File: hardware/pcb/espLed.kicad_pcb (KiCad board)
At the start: 2 copper layers, 32.3 x 36.6 mm, 23 parts, among them J1 led_strip, J2 flashing, J3 power, Q1 IRF9310TRPBF, Q2 AO3400A, Q3 AO3400A, Q4 AO3400A, SW1 reset, SW2 flash, U1 AMS1117-3.3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

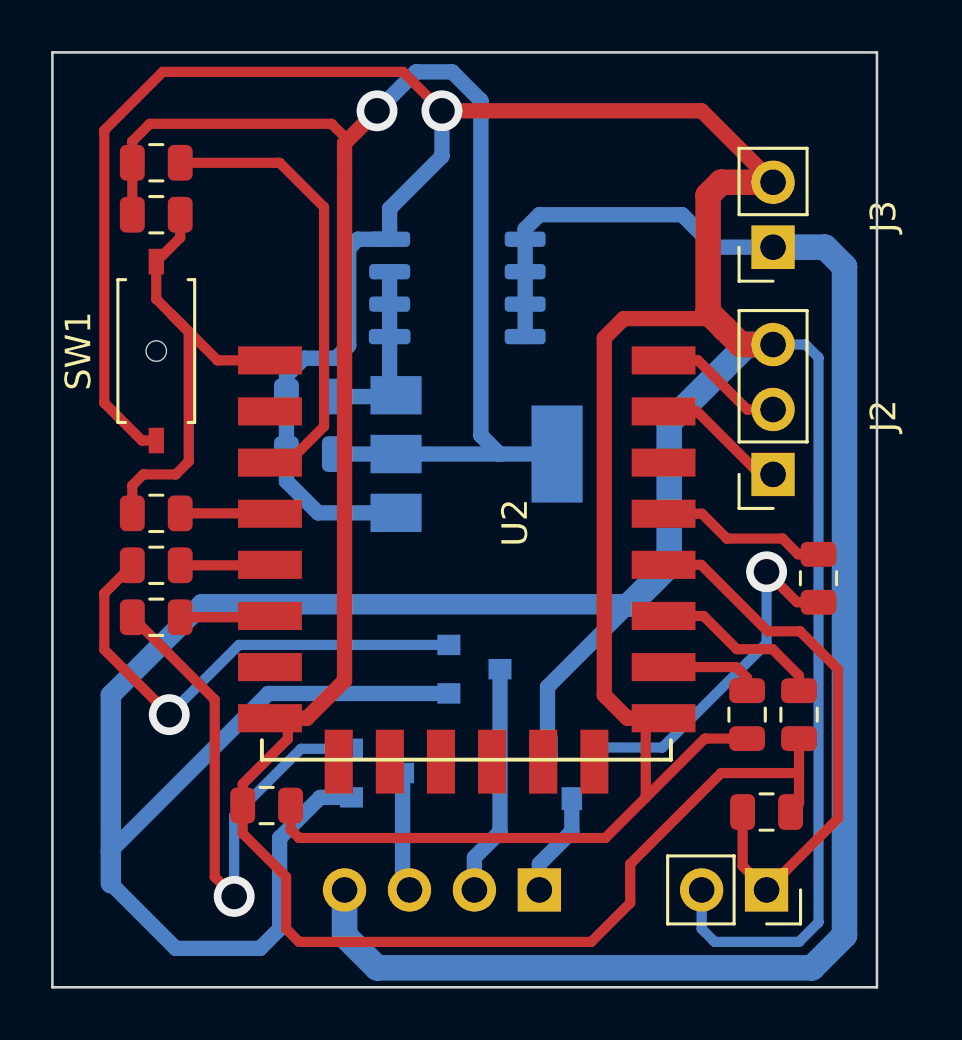
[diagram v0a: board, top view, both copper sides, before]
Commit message: reroute GND of the 'flash' jumper to fit leds' 12v tighter
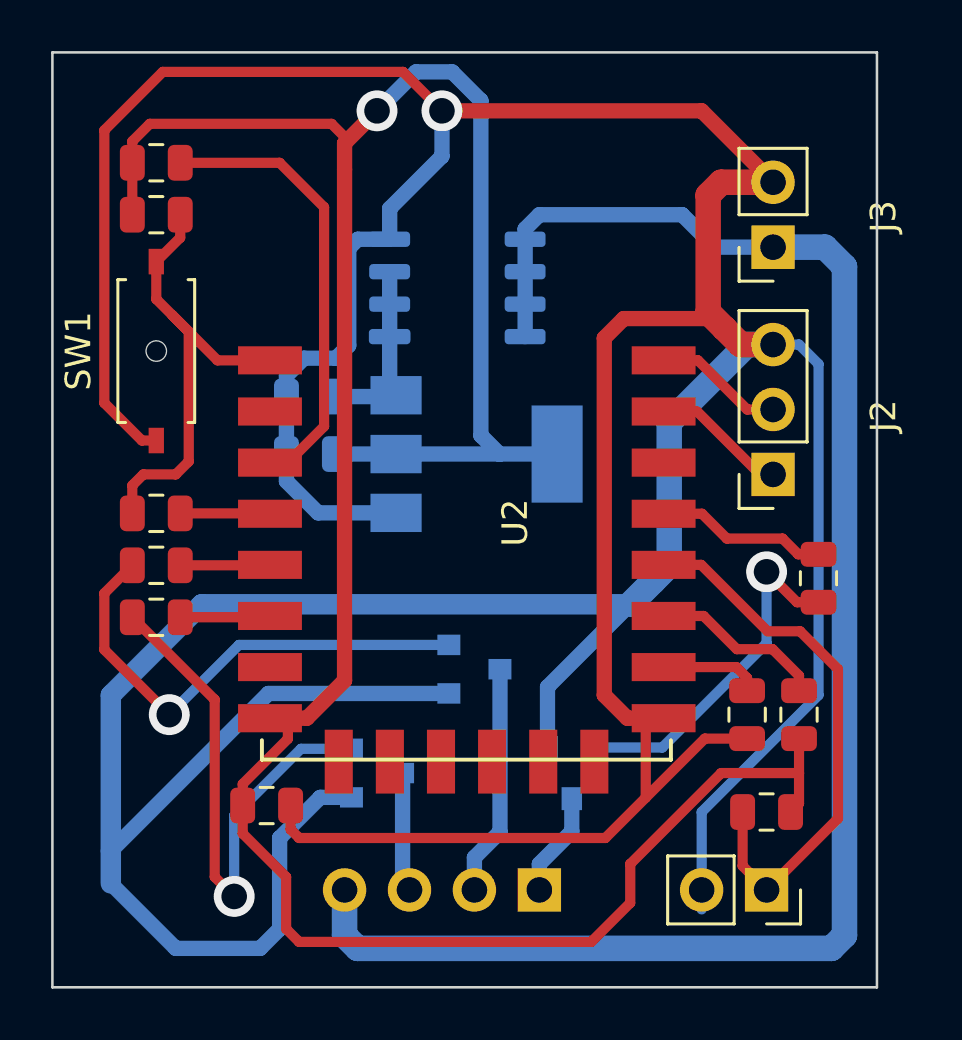
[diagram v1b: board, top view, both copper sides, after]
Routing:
- net GND: track 233.4 -> 227.3 mm
- net /12v_in: track 66.3 -> 65.7 mm
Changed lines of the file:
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@@
     (thickness 1.6)
     (drawings 6)
-    (tracks 207)
+    (tracks 205)
     (zones 0)
     (modules 23)
@@
   )
   (setup
-    (last_trace_width 0.6)
+    (last_trace_width 0.4)
     (user_trace_width 0.4)
     (user_trace_width 0.6)
@@
   (segment (start 188.590501 133.0175) (end 186.28 135.328001) (width 0.4) (layer F.Cu) (net 1))
   (segment (start 190.246 133.0175) (end 188.590501 133.0175) (width 0.4) (layer F.Cu) (net 1))
-  (segment (start 192.532 117.602) (end 191.262 117.602) (width 0.4) (layer B.Cu) (net 1))
-  (segment (start 193.04 118.11) (end 192.532 117.602) (width 0.4) (layer B.Cu) (net 1))
-  (segment (start 193.04 140.208) (end 193.04 118.11) (width 0.4) (layer B.Cu) (net 1))
-  (segment (start 192.278 140.97) (end 193.04 140.208) (width 0.4) (layer B.Cu) (net 1))
-  (segment (start 188.976 140.97) (end 192.278 140.97) (width 0.4) (layer B.Cu) (net 1))
-  (segment (start 188.468 140.462) (end 188.976 140.97) (width 0.4) (layer B.Cu) (net 1))
-  (segment (start 188.468 138.938) (end 188.468 140.462) (width 0.4) (layer B.Cu) (net 1))
   (segment (start 189.23 111.252) (end 191.262 111.252) (width 1) (layer F.Cu) (net 1))
   (segment (start 188.722 111.76) (end 189.23 111.252) (width 1) (layer F.Cu) (net 1))
@@
   (segment (start 165.354 137.414) (end 165.354 131.318) (width 0.8) (layer B.Cu) (net 1))
   (segment (start 165.354 138.684) (end 165.354 137.414) (width 0.8) (layer B.Cu) (net 1))
+  (segment (start 193.04 131.318) (end 188.468 135.89) (width 0.4) (layer B.Cu) (net 1))
+  (segment (start 188.468 135.89) (end 188.468 138.938) (width 0.4) (layer B.Cu) (net 1))
+  (segment (start 193.04 118.364) (end 193.04 131.318) (width 0.4) (layer B.Cu) (net 1))
+  (segment (start 192.278 117.602) (end 193.04 118.364) (width 0.4) (layer B.Cu) (net 1))
+  (segment (start 191.262 117.602) (end 192.278 117.602) (width 0.4) (layer B.Cu) (net 1))
   (segment (start 174.0995 119.636) (end 176.462 119.636) (width 0.6) (layer B.Cu) (net 2))
   (segment (start 176.262 117.291) (end 176.262 114.751) (width 0.6) (layer B.Cu) (net 2))
@@
   (segment (start 188.292 120.22) (end 190.754 122.682) (width 0.4) (layer F.Cu) (net 8))
   (segment (start 186.28 120.22) (end 188.292 120.22) (width 0.4) (layer F.Cu) (net 8))
-  (segment (start 175.768 141.986) (end 174.498 140.716) (width 1) (layer B.Cu) (net 9))
-  (segment (start 192.786 141.986) (end 175.768 141.986) (width 1) (layer B.Cu) (net 9))
-  (segment (start 194.056 140.716) (end 192.786 141.986) (width 1) (layer B.Cu) (net 9))
-  (segment (start 194.056 114.554) (end 194.056 140.716) (width 1) (layer B.Cu) (net 9))
-  (segment (start 174.498 140.716) (end 174.498 138.938) (width 1) (layer B.Cu) (net 9))
-  (segment (start 193.294 113.792) (end 194.056 114.554) (width 1) (layer B.Cu) (net 9))
-  (segment (start 191.262 113.792) (end 193.294 113.792) (width 1) (layer B.Cu) (net 9))
   (segment (start 181.562 113.481) (end 181.562 117.291) (width 0.6) (layer B.Cu) (net 9))
   (segment (start 181.562 113.078) (end 181.562 113.481) (width 0.6) (layer B.Cu) (net 9))
@@
   (segment (start 187.706 112.522) (end 182.118 112.522) (width 0.6) (layer B.Cu) (net 9))
   (segment (start 191.262 113.792) (end 188.976 113.792) (width 0.6) (layer B.Cu) (net 9))
+  (segment (start 174.498 140.716) (end 174.498 138.938) (width 1) (layer B.Cu) (net 9))
+  (segment (start 175.006 141.224) (end 174.498 140.716) (width 1) (layer B.Cu) (net 9))
+  (segment (start 193.548 141.224) (end 175.006 141.224) (width 1) (layer B.Cu) (net 9))
+  (segment (start 194.056 114.554) (end 194.056 140.716) (width 1) (layer B.Cu) (net 9))
+  (segment (start 193.294 113.792) (end 194.056 114.554) (width 1) (layer B.Cu) (net 9))
+  (segment (start 194.056 140.716) (end 193.548 141.224) (width 1) (layer B.Cu) (net 9))
+  (segment (start 191.262 113.792) (end 193.294 113.792) (width 1) (layer B.Cu) (net 9))
   (via (at 191.008 126.492) (size 1.6) (drill 1) (layers F.Cu B.Cu) (net 10))
   (segment (start 192.1995 127.6835) (end 191.008 126.492) (width 0.4) (layer F.Cu) (net 10))

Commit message: fix the board outline
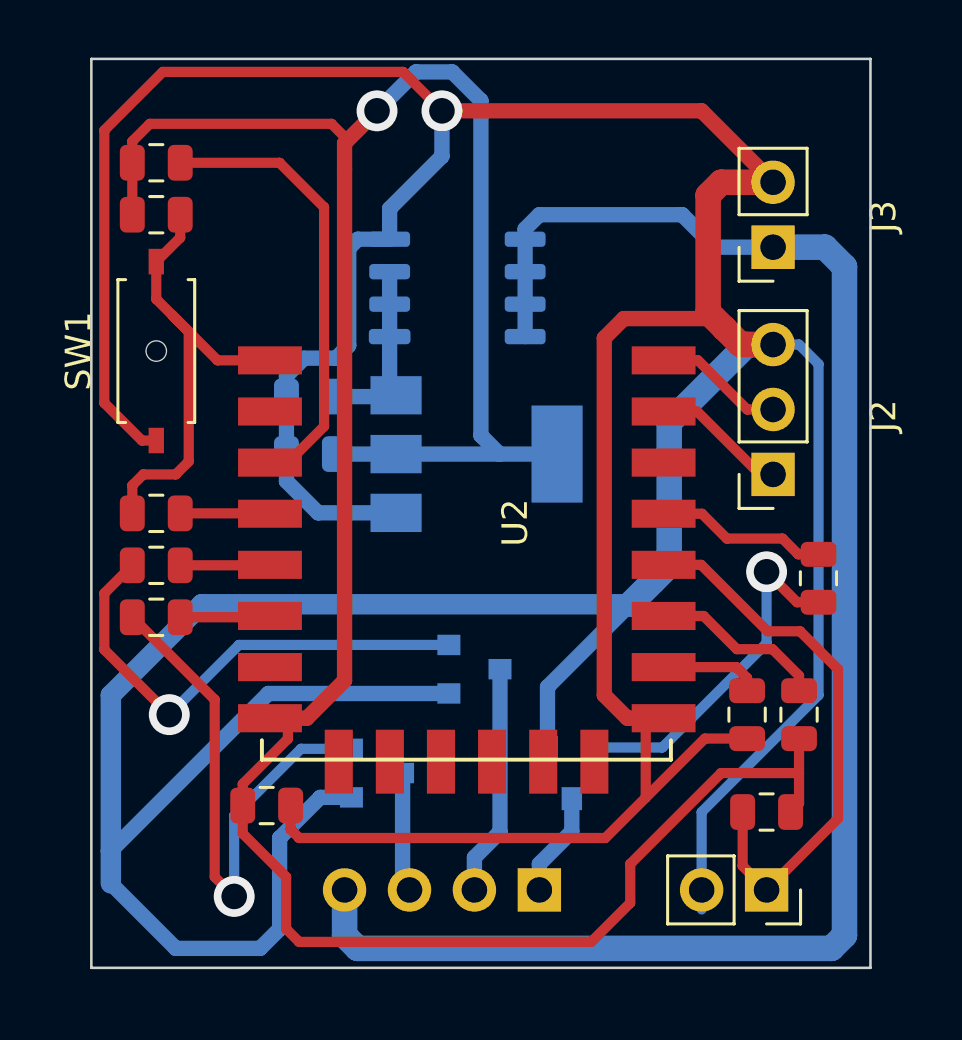
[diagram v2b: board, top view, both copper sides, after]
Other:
- board size 32.3 x 36.6 mm -> 30.5 x 35.6 mm
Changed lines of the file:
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@@
     )
   )
-  (dimension 36.576 (width 0.15) (layer Dwgs.User)
-    (gr_text "36,576 mm" (at 199.674 124.46 270) (layer Dwgs.User)
+  (dimension 30.48 (width 0.15) (layer Dwgs.User)
+    (gr_text "30,480 mm" (at 179.832 103.348) (layer Dwgs.User)
       (effects (font (size 1 1) (thickness 0.15)))
     )
-    (feature1 (pts (xy 195.326 142.748) (xy 198.960421 142.748)))
-    (feature2 (pts (xy 195.326 106.172) (xy 198.960421 106.172)))
-    (crossbar (pts (xy 198.374 106.172) (xy 198.374 142.748)))
-    (arrow1a (pts (xy 198.374 142.748) (xy 197.787579 141.621496)))
-    (arrow1b (pts (xy 198.374 142.748) (xy 198.960421 141.621496)))
-    (arrow2a (pts (xy 198.374 106.172) (xy 197.787579 107.298504)))
-    (arrow2b (pts (xy 198.374 106.172) (xy 198.960421 107.298504)))
+    (feature1 (pts (xy 195.072 106.426) (xy 195.072 104.061579)))
+    (feature2 (pts (xy 164.592 106.426) (xy 164.592 104.061579)))
+    (crossbar (pts (xy 164.592 104.648) (xy 195.072 104.648)))
+    (arrow1a (pts (xy 195.072 104.648) (xy 193.945496 105.234421)))
+    (arrow1b (pts (xy 195.072 104.648) (xy 193.945496 104.061579)))
+    (arrow2a (pts (xy 164.592 104.648) (xy 165.718504 105.234421)))
+    (arrow2b (pts (xy 164.592 104.648) (xy 165.718504 104.061579)))
   )
-  (dimension 32.258 (width 0.15) (layer Dwgs.User)
-    (gr_text "32,258 mm" (at 179.197 102.586) (layer Dwgs.User)
+  (dimension 35.56 (width 0.15) (layer Dwgs.User)
+    (gr_text "35,560 mm" (at 198.15 124.206 270) (layer Dwgs.User)
       (effects (font (size 1 1) (thickness 0.15)))
     )
-    (feature1 (pts (xy 195.326 106.172) (xy 195.326 103.299579)))
-    (feature2 (pts (xy 163.068 106.172) (xy 163.068 103.299579)))
-    (crossbar (pts (xy 163.068 103.886) (xy 195.326 103.886)))
-    (arrow1a (pts (xy 195.326 103.886) (xy 194.199496 104.472421)))
-    (arrow1b (pts (xy 195.326 103.886) (xy 194.199496 103.299579)))
-    (arrow2a (pts (xy 163.068 103.886) (xy 164.194504 104.472421)))
-    (arrow2b (pts (xy 163.068 103.886) (xy 164.194504 103.299579)))
+    (feature1 (pts (xy 195.072 141.986) (xy 197.436421 141.986)))
+    (feature2 (pts (xy 195.072 106.426) (xy 197.436421 106.426)))
+    (crossbar (pts (xy 196.85 106.426) (xy 196.85 141.986)))
+    (arrow1a (pts (xy 196.85 141.986) (xy 196.263579 140.859496)))
+    (arrow1b (pts (xy 196.85 141.986) (xy 197.436421 140.859496)))
+    (arrow2a (pts (xy 196.85 106.426) (xy 196.263579 107.552504)))
+    (arrow2b (pts (xy 196.85 106.426) (xy 197.436421 107.552504)))
   )
-  (gr_line (start 195.326 106.172) (end 195.326 142.748) (layer Edge.Cuts) (width 0.1))
-  (gr_line (start 163.068 106.172) (end 195.326 106.172) (layer Edge.Cuts) (width 0.1))
-  (gr_line (start 163.068 142.748) (end 163.068 106.172) (layer Edge.Cuts) (width 0.1))
-  (gr_line (start 195.326 142.748) (end 163.068 142.748) (layer Edge.Cuts) (width 0.1))
+  (gr_line (start 195.072 106.426) (end 195.072 141.986) (layer Edge.Cuts) (width 0.1))
+  (gr_line (start 164.592 106.426) (end 195.072 106.426) (layer Edge.Cuts) (width 0.1))
+  (gr_line (start 164.592 141.986) (end 164.592 106.426) (layer Edge.Cuts) (width 0.1))
+  (gr_line (start 195.072 141.986) (end 164.592 141.986) (layer Edge.Cuts) (width 0.1))
   (segment (start 172.2245 122.9485) (end 172.2245 121.886) (width 0.6) (layer B.Cu) (net 1))
   (segment (start 173.462 124.186) (end 172.2245 122.9485) (width 0.6) (layer B.Cu) (net 1))

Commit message: fix ESP's 3d model and move led connector to the top layer (just visual)
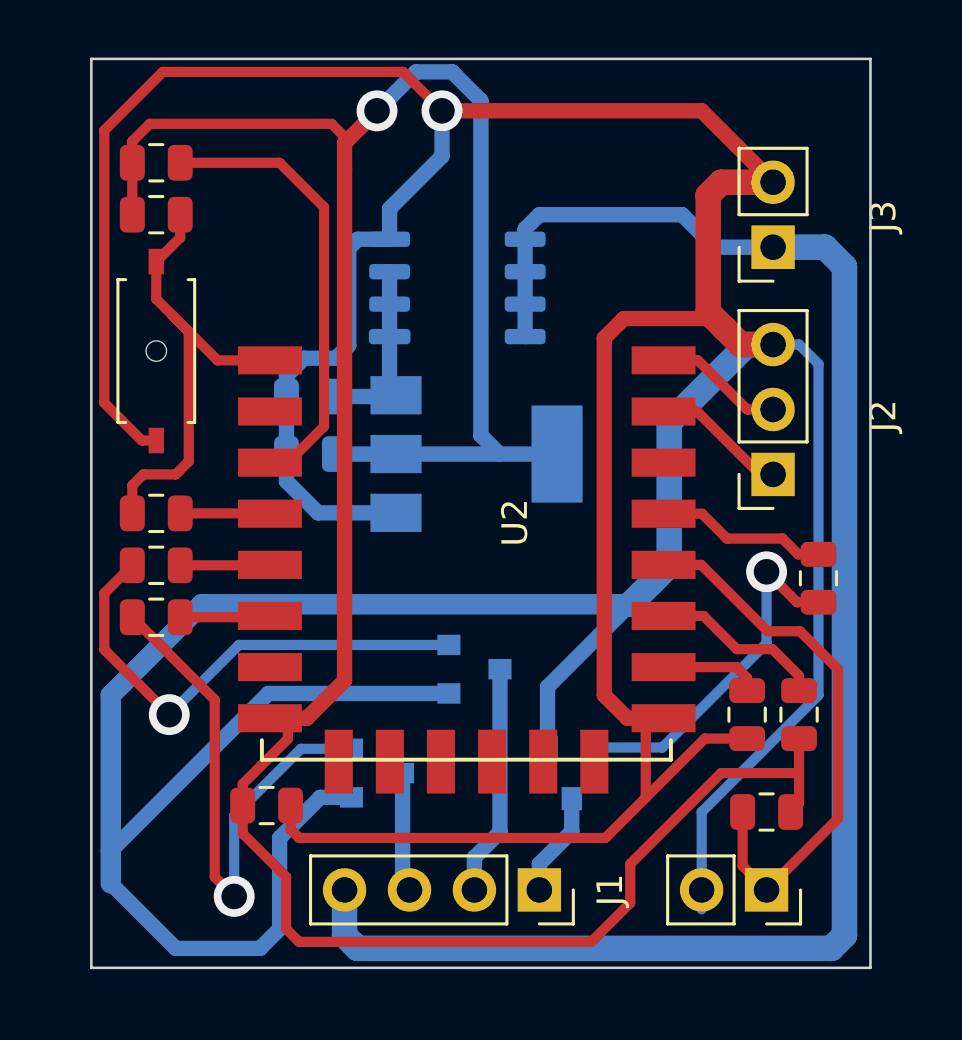
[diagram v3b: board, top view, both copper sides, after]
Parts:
- J1: moved to F.Cu
- turned J1 to 270 degrees
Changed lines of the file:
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@@
+      (rotate (xyz 0 0 0))
+    )
+    (model ${KIPRJMOD}/libs/kicad-ESP8266/ESP8266.3dshapes/ESP-12-E-better.wrl
+      (at (xyz 0 0 0))
+      (scale (xyz 1 1 1))
       (rotate (xyz 0 0 0))
     )
@@
     (tags "Tactile Switch")
     (attr smd)
-    (fp_text reference SW1 (at 0 -3.048 90) (layer F.SilkS)
-      (effects (font (size 1 1) (thickness 0.15)))
-    )
-    (fp_text value reset (at -0.254 -2.286 90) (layer F.Fab)
+    (fp_text reference SW1 (at 0 -3.048 90) (layer F.SilkS) hide
+      (effects (font (size 1 1) (thickness 0.15)))
+    )
+    (fp_text value reset (at -0.254 -2.286 90) (layer F.Fab) hide
       (effects (font (size 1 1) (thickness 0.15)))
     )
@@
     )
   )
-  (module Connector_PinSocket_2.54mm:PinSocket_1x04_P2.54mm_Vertical (layer B.Cu)
-    (at 182.118 138.938 90)
+  (module Connector_PinSocket_2.54mm:PinSocket_1x04_P2.54mm_Vertical (layer F.Cu)
+    (at 182.118 138.938 270)
     (descr "Through hole straight socket strip, 1x04, 2.54mm pitch, single row (from Kicad 4.0.7), script generated")
     (tags "Through hole socket strip THT 1x04 2.54mm single row")
-    (fp_text reference J1 (at 0 2.77 90) (layer B.SilkS)
-      (effects (font (size 1 1) (thickness 0.15)) (justify mirror))
-    )
-    (fp_text value led_strip (at 0 -10.39 90) (layer B.Fab)
-      (effects (font (size 1 1) (thickness 0.15)) (justify mirror))
-    )
-    (fp_line (start -1.27 1.27) (end 0.635 1.27) (layer B.Fab) (width 0.1))
-    (fp_line (start 0.635 1.27) (end 1.27 0.635) (layer B.Fab) (width 0.1))
-    (fp_line (start 1.27 0.635) (end 1.27 -8.89) (layer B.Fab) (width 0.1))
-    (fp_line (start 1.27 -8.89) (end -1.27 -8.89) (layer B.Fab) (width 0.1))
-    (fp_line (start -1.27 -8.89) (end -1.27 1.27) (layer B.Fab) (width 0.1))
-    (fp_line (start -1.33 -1.27) (end 1.33 -1.27) (layer B.SilkS) (width 0.12))
-    (fp_line (start -1.33 -1.27) (end -1.33 -8.95) (layer B.SilkS) (width 0.12))
-    (fp_line (start -1.33 -8.95) (end 1.33 -8.95) (layer B.SilkS) (width 0.12))
-    (fp_line (start 1.33 -1.27) (end 1.33 -8.95) (layer B.SilkS) (width 0.12))
-    (fp_line (start 1.33 1.33) (end 1.33 0) (layer B.SilkS) (width 0.12))
-    (fp_line (start 0 1.33) (end 1.33 1.33) (layer B.SilkS) (width 0.12))
-    (fp_line (start -1.8 1.8) (end 1.75 1.8) (layer B.CrtYd) (width 0.05))
-    (fp_line (start 1.75 1.8) (end 1.75 -9.4) (layer B.CrtYd) (width 0.05))
-    (fp_line (start 1.75 -9.4) (end -1.8 -9.4) (layer B.CrtYd) (width 0.05))
-    (fp_line (start -1.8 -9.4) (end -1.8 1.8) (layer B.CrtYd) (width 0.05))
-    (fp_text user %R (at 0 -3.81 180) (layer B.Fab)
-      (effects (font (size 1 1) (thickness 0.15)) (justify mirror))
-    )
-    (pad 1 thru_hole rect (at 0 0 90) (size 1.7 1.7) (drill 1) (layers *.Cu *.Mask)
+    (fp_text reference J1 (at 0 -2.77 270) (layer F.SilkS)
+      (effects (font (size 1 1) (thickness 0.15)))
+    )
+    (fp_text value led_strip (at 0 10.39 270) (layer F.Fab)
+      (effects (font (size 1 1) (thickness 0.15)))
+    )
+    (fp_line (start -1.27 -1.27) (end 0.635 -1.27) (layer F.Fab) (width 0.1))
+    (fp_line (start 0.635 -1.27) (end 1.27 -0.635) (layer F.Fab) (width 0.1))
+    (fp_line (start 1.27 -0.635) (end 1.27 8.89) (layer F.Fab) (width 0.1))
+    (fp_line (start 1.27 8.89) (end -1.27 8.89) (layer F.Fab) (width 0.1))
+    (fp_line (start -1.27 8.89) (end -1.27 -1.27) (layer F.Fab) (width 0.1))
+    (fp_line (start -1.33 1.27) (end 1.33 1.27) (layer F.SilkS) (width 0.12))
+    (fp_line (start -1.33 1.27) (end -1.33 8.95) (layer F.SilkS) (width 0.12))
+    (fp_line (start -1.33 8.95) (end 1.33 8.95) (layer F.SilkS) (width 0.12))
+    (fp_line (start 1.33 1.27) (end 1.33 8.95) (layer F.SilkS) (width 0.12))
+    (fp_line (start 1.33 -1.33) (end 1.33 0) (layer F.SilkS) (width 0.12))
+    (fp_line (start 0 -1.33) (end 1.33 -1.33) (layer F.SilkS) (width 0.12))
+    (fp_line (start -1.8 -1.8) (end 1.75 -1.8) (layer F.CrtYd) (width 0.05))
+    (fp_line (start 1.75 -1.8) (end 1.75 9.4) (layer F.CrtYd) (width 0.05))
+    (fp_line (start 1.75 9.4) (end -1.8 9.4) (layer F.CrtYd) (width 0.05))
+    (fp_line (start -1.8 9.4) (end -1.8 -1.8) (layer F.CrtYd) (width 0.05))
+    (fp_text user %R (at 0 3.81 180) (layer F.Fab)
+      (effects (font (size 1 1) (thickness 0.15)))
+    )
+    (pad 1 thru_hole rect (at 0 0 270) (size 1.7 1.7) (drill 1) (layers *.Cu *.Mask)
       (net 6 /led1_out))
-    (pad 2 thru_hole oval (at 0 -2.54 90) (size 1.7 1.7) (drill 1) (layers *.Cu *.Mask)
+    (pad 2 thru_hole oval (at 0 2.54 270) (size 1.7 1.7) (drill 1) (layers *.Cu *.Mask)
       (net 5 /led2_out))
-    (pad 3 thru_hole oval (at 0 -5.08 90) (size 1.7 1.7) (drill 1) (layers *.Cu *.Mask)
+    (pad 3 thru_hole oval (at 0 5.08 270) (size 1.7 1.7) (drill 1) (layers *.Cu *.Mask)
       (net 4 /led3_out))
-    (pad 4 thru_hole oval (at 0 -7.62 90) (size 1.7 1.7) (drill 1) (layers *.Cu *.Mask)
+    (pad 4 thru_hole oval (at 0 7.62 270) (size 1.7 1.7) (drill 1) (layers *.Cu *.Mask)
       (net 9 /12v_in))
     (model ${KISYS3DMOD}/Connector_PinSocket_2.54mm.3dshapes/PinSocket_1x04_P2.54mm_Vertical.wrl
